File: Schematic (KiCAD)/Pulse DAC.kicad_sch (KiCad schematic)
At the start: 72 parts

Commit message: - Pulse DAC logic is now complete.  - The 4-bit adders are verified correct using Excel.    - This revealed 1 tracing error and also 3 XNOR gates that are actually XOR in this case.  - Now including a PDF version of the schematic.
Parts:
- removed B72, B80: XNOR_2, symbol MMC5:XNOR_2
- added B46, B63, B66, B67, B71, B79, B87, B88, B89, B94, C13, F29, G17: INVERT, symbol MMC5:INVERT
- added B62: NOR_4, symbol MMC5:NOR_4
- added B64, B70, B74, B76, B77, B78, B83, B86, G27, G88: NAND_2, symbol MMC5:NAND_2
- added B65, B68: NAND_3, symbol MMC5:NAND_3
- added B72, B80: XOR_2, symbol MMC5:XOR_2
- added B75: NOR_3, symbol MMC5:NOR_3
- added B81, B82: NOR_2, symbol MMC5:NOR_2
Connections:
- net Pulse_1_With_Duty{F32}: now also G88. (X)
- net Pulse_2_With_Duty{G20}: now also G27. (X)
- net Pulse_DAC_Bit_4: now also B80. (X); no longer B61. (X)
- net Pulse_DAC_Bit_5: now also B72. (X)
- net Pulse_DAC_Bit_7: now also B61. (X)
- net Pulse_1_DAC.2{F30}: now reaches F30. (X)
- net Pulse_1_DAC.2{F30}: now also B73. (X), B74. (X); no longer G89. (X)
- net at H45. (X): now also H66. (X); no longer H44. (X)
- net at H66. (X): now also H63. (X); no longer H45. (X)
- net Pulse_DACs_Nor.0{B84}: now reaches B54. (X)
- net Pulse_DACs_Nor.0{B84}: now also B50. (X), B84. (X), B65. (X), B76. (X), B81. (X)
- net at B59. (X): now also B61. (X); no longer B54. (X)
- net at H71. (X): now also H74. (X); no longer H70. (X)
- net at H74. (X): now also H75. (X); no longer H71. (X)
- net at H73. (X): now also H72. (X); no longer H74. (X)
- net at H47. (X): now also H46. (X); no longer H74. (X)
- net at H75. (X): now also H80. (/Q3); no longer H74. (X)
- net at H58. (X): now also H80. (/Q3); no longer H57. (X)
- net Pulse_DACs_Nor.3{B53}: now reaches B61. (X)
- net Pulse_DACs_Nor.3{B53}: now also B53. (X), C13. (X); no longer B59. (X)
- net at B57. (X): now also B61. (X); no longer B56. (X)
- net at H43. (X): now also H42. (X); no longer H57. (X)
- net Pulse_2_DAC.2{G18}: now reaches B73. (X), G18. (X)
- net Pulse_2_DAC.2{G18}: now also B74. (X)
- net Pulse_DACs_Nor.2{B73}: now reaches B73. (X)
- net Pulse_DACs_Nor.2{B73}: now also B56. (X), B62. (X), B87. (X); no longer F30. (X)
- net at H49. (X): now also H50. (X); no longer H48. (X)
- net at H50. (X): now also H51. (X); no longer H41. (X)
- net at H51. (X): now also H80. (/Q3); no longer H50. (X)
- net at H57. (X): now also H56. (X); no longer H54. (X)
- net at H56. (X): now also H55. (X); no longer H57. (X)
- net Pulse_2_DAC.3{G19}: now reaches G19. (X)
- net Pulse_2_DAC.3{G19}: now also B45. (X), B53. (X); no longer G25. (X)
- net Pulse_2_DAC.0{G24}: now reaches G24. (X)
- net Pulse_2_DAC.0{G24}: now also B84. (X), B85. (X); no longer G28. (X)
- net Pulse_DACs_Nand.3{B45}: now reaches B45. (X), B56. (X)
- net Pulse_DACs_Nand.3{B45}: now also B52. (X), B54. (X), B55. (X), B86. (X)
- net Pulse_1_DAC.3{F31}: now reaches B45. (X), F31. (X)
- net Pulse_1_DAC.3{F31}: now also B53. (X)
- net at H67. (X): now also H66. (X); no longer H80. (/Q3)
- net Pulse_DACs_Nor.1{B82}: now reaches B55. (X)
- net Pulse_DACs_Nor.1{B82}: now also B64. (X), B75. (X), B82. (X), B88. (X)
- net at B58. (X): now also B61. (X); no longer B55. (X)
- net Pulse_DACs_Nand.0{B85}: now reaches B49. (X), B85. (X)
- net Pulse_DACs_Nand.0{B85}: now also B52. (X), B68. (X), B77. (X), B81. (X)
- net Pulse_1_DAC.0{F28}: now reaches F28. (X)
- net Pulse_1_DAC.0{F28}: now also B84. (X), B85. (X); no longer G87. (X)
- net at H65. (X): now also H64. (X); no longer H66. (X)
- net at B60. (X): now also B61. (X); no longer B52. (X)
- new net: F30. (X), G89. (X)
- new net: H44. (X), H45. (X)
- new net: B54. (X), B59. (X)
- new net: B72. (X), B75. (X)
- new net: B75. (X), B94. (X)
- new net: B75. (X), B89. (X)
- new net: H38. (X), H48. (X), H53. (X), H55. (X), H61. (X), H62. (X), H64. (X), H69. (X), H70. (X), H72. (X)
- new net: H70. (X), H71. (X)
- new net: H69. (X), H70. (X)
- new net: H38. (X), H39. (X), H40. (X), H42. (X), H44. (X), H46. (X)
- new net: B86. (X), C13. (X)
- new net: H73. (X), H74. (X)
- new net: H47. (X), H74. (X)
- new net: H57. (X), H58. (X)
- new net: B56. (X), B57. (X)
- new net: H43. (X), H57. (X)
- new net: B76. (X), B94. (X)
- new net: B78. (X), B88. (X)
- new net: B47. (X), B62. (X)
- new net: B46. (X), B47. (X)
- new net: B71. (X), B72. (X)
- new net: B70. (X), B71. (X)
- new net: H61. (X), H62. (X)
- new net: H62. (X), H63. (X)
- new net: H48. (X), H49. (X)
- new net: H41. (X), H50. (X)
- new net: H54. (X), H57. (X)
- new net: G18. (X), G26. (X)
- new net: G19. (X), G25. (X)
- new net: F29. (X), G88. (X)
- new net: G24. (X), G28. (X)
- new net: B63. (X), B64. (X)
- new net: B62. (X), B63. (X)
- new net: B70. (X), B87. (X)
- new net: B80. (X), B81. (X)
- new net: B67. (X), B68. (X)
- new net: B62. (X), B67. (X)
- new net: H67. (X), H80. (/Q3)
- new net: B46. (X), B86. (X)
- new net: B55. (X), B58. (X)
- new net: B77. (X), B89. (X)
- new net: B65. (X), B66. (X)
- new net: B62. (X), B66. (X)
- new net: F28. (X), G87. (X)
- new net: B79. (X), B80. (X)
- new net: G17. (X), G27. (X)
- new net: H65. (X), H66. (X)
- new net: B52. (X), B60. (X)
- new net: F31. (X), G90. (X)
- new net: B49. (X), B51. (X)
- new net: B49. (X), B50. (X)
- new net: B78. (X), B79. (X)
- new net Pulse_1_DAC.1{F29}: B82. (X), B83. (X), F29. (X)
- new net Pulse_1_Vol/Env.1{H102}: G88. (X)
- new net Pulse_2_DAC.1{G17}: B82. (X), B83. (X), G17. (X)
- new net Pulse_2_Vol/Env.1{F23}: G27. (X)
- new net Pulse_DACs_Nand.1{B83}: B52. (X), B54. (X), B65. (X), B68. (X), B76. (X), B77. (X), B78. (X), B83. (X)
- new net Pulse_DACs_Nand.2{B74}: B52. (X), B54. (X), B55. (X), B64. (X), B65. (X), B68. (X), B70. (X), B74. (X)
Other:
- note added: "$5015 Write Register Pulse 1&2 Status"
- note added: "4-bit Adder Adding Pulse 1&2 DACs"
- note added: "B80,B72,B47: Though they look like XNOR gates from elsewhere, logically these must be XOR."
- note added: "Components for 4-bit Adder"
- note added: "Don't know what this is yet But it is important."
- note added: "Note: The adder's logic is verified correct in Pulse DAC Adder Logic.xlsx"
- note added: "Pulse 1&2 Individual 4-bit DAC Outputs"
- note added: "This logic amounts to XOR"
- note removed: "$5015 Register Pulse 1&2 Status"
- moved on the sheet: B45, B47, B49, B50, B51, B52, B53, B54, B55, B56, B57, B58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

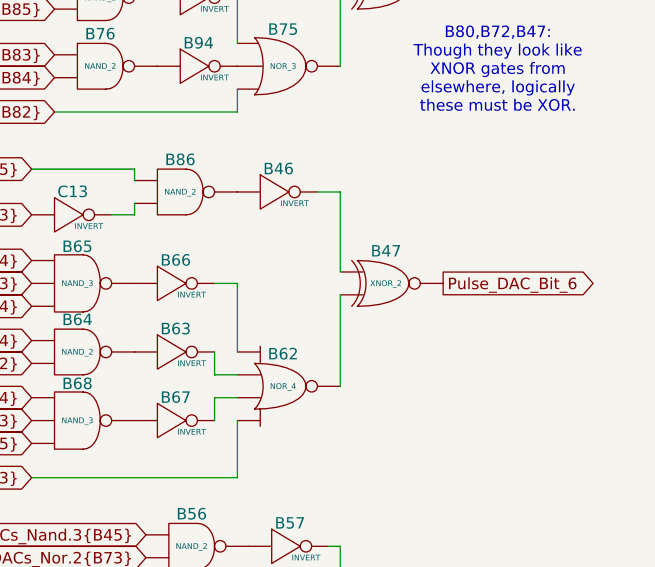
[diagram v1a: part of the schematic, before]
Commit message: Schematic Updates:  - Added all 10-bit CHR banking registers $5120 - $512B, including where all 10 bits come from when written.  - Added 8-bit CHR bank register $5202, which is the bank used when rendering the V-Split region.    + V-Split seems to always be 8-bit, 8kB bank regardless of CHR mode.  The wiki doesn't say that and I don't know for sure.  - Added decoding logic that activates the correct CHR bank for CHR A10, A11, A12 (corresponding to columns AV, AW, AX).  - Noted, AX15 activates $5202 CHR Bank for V-Split region.  AX16 activates CHR Bank from data stored in ExRAM for extended attributes.  Therefore, AX15 driven by AT1 High means we specifically are in v-split region, and not extended attribute mode.  With this knowledge, backtracking up the chain from AT1 to N14 sheds very useful insight what the 3-bit shift register at N11/N12/N13 is doing.  We now know that N14 goes low specifically for pattern table fetches when rendering the V-split region, and does not appear dual-purposed for extended attribute fetch sequencing.  This may seem rather subtle or unimportant, but it is a good advancement for higher level understanding what that mysterious shift register might be doing.
SVG Trace Updates:
 - Registers $5120, 5121, 5122, 5123 (first 4 CHR bank register), the outputs were labeled in reverse order.
 - Register $5130 (highest CHR bank bits), the outputs were labeled with backwards polarity.  The error was not having taken into account that the CPU data bus input to the latches came already inverted to begin with.
 - Still wrong: Cell AV7, 2-input NAND gate.  One of the inputs is missing and it logically should be driven by AS19 like the 4 cells to its direct right.  I can't quite make out how it makes that connection.
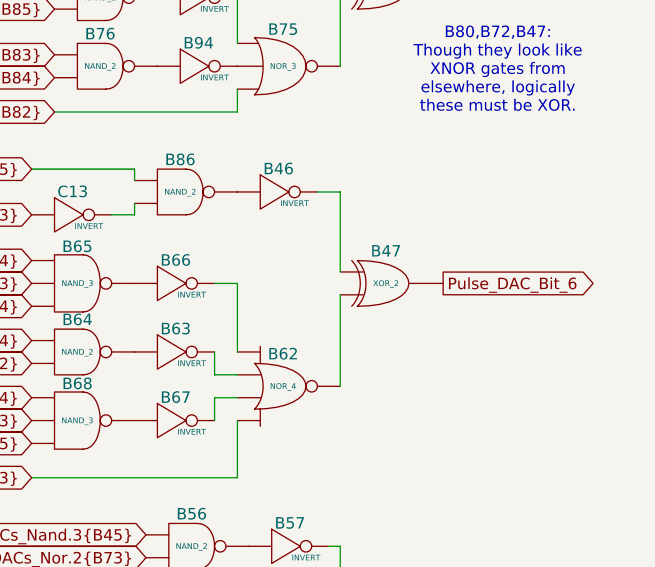
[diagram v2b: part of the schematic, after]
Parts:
- removed B47: XNOR_2, symbol MMC5:XNOR_2
- added B47: XOR_2, symbol MMC5:XOR_2
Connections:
- net Pulse_DAC_Bit_6: now also B47. (X)
- net at H45. (X): now also H66. (X); no longer H44. (X)
- net at H66. (X): now also H63. (X); no longer H45. (X)
- net at B59. (X): now also B61. (X); no longer B54. (X)
- net at B94. (X): now also B76. (X); no longer B75. (X)
- net at B89. (X): now also B77. (X); no longer B75. (X)
- net at H71. (X): now also H74. (X); no longer H70. (X)
- net at H74. (X): now also H75. (X); no longer H71. (X)
- net at H73. (X): now also H72. (X); no longer H74. (X)
- net at H47. (X): now also H46. (X); no longer H74. (X)
- net at H75. (X): now also H80. (/Q3); no longer H74. (X)
- net at H58. (X): now also H80. (/Q3); no longer H57. (X)
- net at B57. (X): now also B61. (X); no longer B56. (X)
- net at H43. (X): now also H42. (X); no longer H57. (X)
- net at B46. (X): now also B86. (X)
- net at B71. (X): now also B70. (X); no longer B72. (X)
- net at H49. (X): now also H50. (X); no longer H48. (X)
- net at H50. (X): now also H51. (X); no longer H41. (X)
- net at H51. (X): now also H80. (/Q3); no longer H50. (X)
- net at H57. (X): now also H56. (X); no longer H54. (X)
- net at H56. (X): now also H55. (X); no longer H57. (X)
- net at B63. (X): now also B62. (X); no longer B64. (X)
- net at B67. (X): now also B62. (X); no longer B68. (X)
- net at H67. (X): now also H66. (X); no longer H80. (/Q3)
- net at B58. (X): now also B61. (X); no longer B55. (X)
- net at B66. (X): now also B62. (X); no longer B65. (X)
- net at B79. (X): now also B78. (X); no longer B80. (X)
- net at H65. (X): now also H64. (X); no longer H66. (X)
- net at B60. (X): now also B61. (X); no longer B52. (X)
- new net: F30. (X), G89. (X)
- new net: H44. (X), H45. (X)
- new net: B54. (X), B59. (X)
- new net: B72. (X), B75. (X)
- new net: B75. (X), B94. (X)
- new net: B75. (X), B89. (X)
- new net: H38. (X), H48. (X), H53. (X), H55. (X), H61. (X), H62. (X), H64. (X), H69. (X), H70. (X), H72. (X)
- new net: H70. (X), H71. (X)
- new net: H69. (X), H70. (X)
- new net: H38. (X), H39. (X), H40. (X), H42. (X), H44. (X), H46. (X)
- new net: B86. (X), C13. (X)
- new net: H73. (X), H74. (X)
- new net: H47. (X), H74. (X)
- new net: H57. (X), H58. (X)
- new net: B56. (X), B57. (X)
- new net: H43. (X), H57. (X)
- new net: B78. (X), B88. (X)
- new net: B71. (X), B72. (X)
- new net: H61. (X), H62. (X)
- new net: H62. (X), H63. (X)
- new net: H48. (X), H49. (X)
- new net: H41. (X), H50. (X)
- new net: H54. (X), H57. (X)
- new net: G18. (X), G26. (X)
- new net: B47. (X), B62. (X)
- new net: B46. (X), B47. (X)
- new net: G19. (X), G25. (X)
- new net: F29. (X), G88. (X)
- new net: G24. (X), G28. (X)
- new net: B63. (X), B64. (X)
- new net: B70. (X), B87. (X)
- new net: B80. (X), B81. (X)
- new net: B67. (X), B68. (X)
- new net: H67. (X), H80. (/Q3)
- new net: B55. (X), B58. (X)
- new net: B65. (X), B66. (X)
- new net: F28. (X), G87. (X)
- new net: B79. (X), B80. (X)
- new net: G17. (X), G27. (X)
- new net: H65. (X), H66. (X)
- new net: B52. (X), B60. (X)
- new net: F31. (X), G90. (X)
- new net: B49. (X), B51. (X)
- new net: B49. (X), B50. (X)

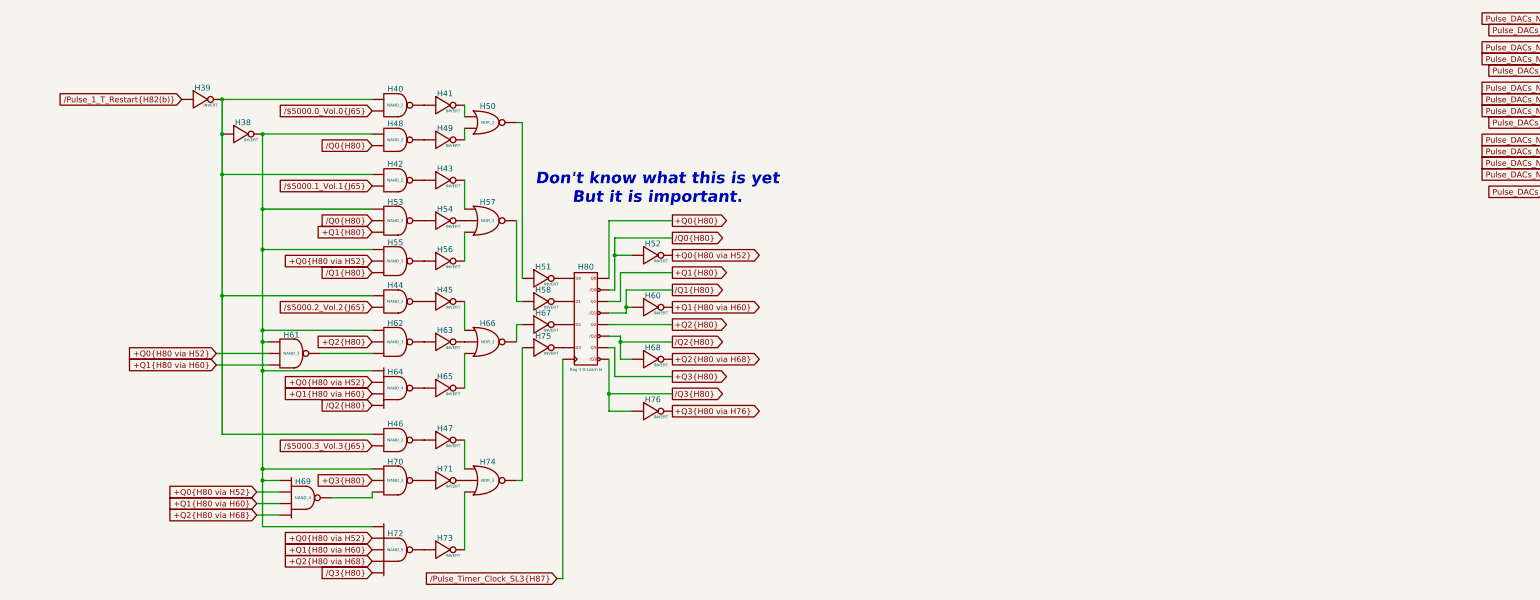
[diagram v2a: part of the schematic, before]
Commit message: - All cells in the left and center areas have now been added into the schematics.  - Changed naming of the PDF files; I was accidentally writing over furrtek's original with my new PDF.
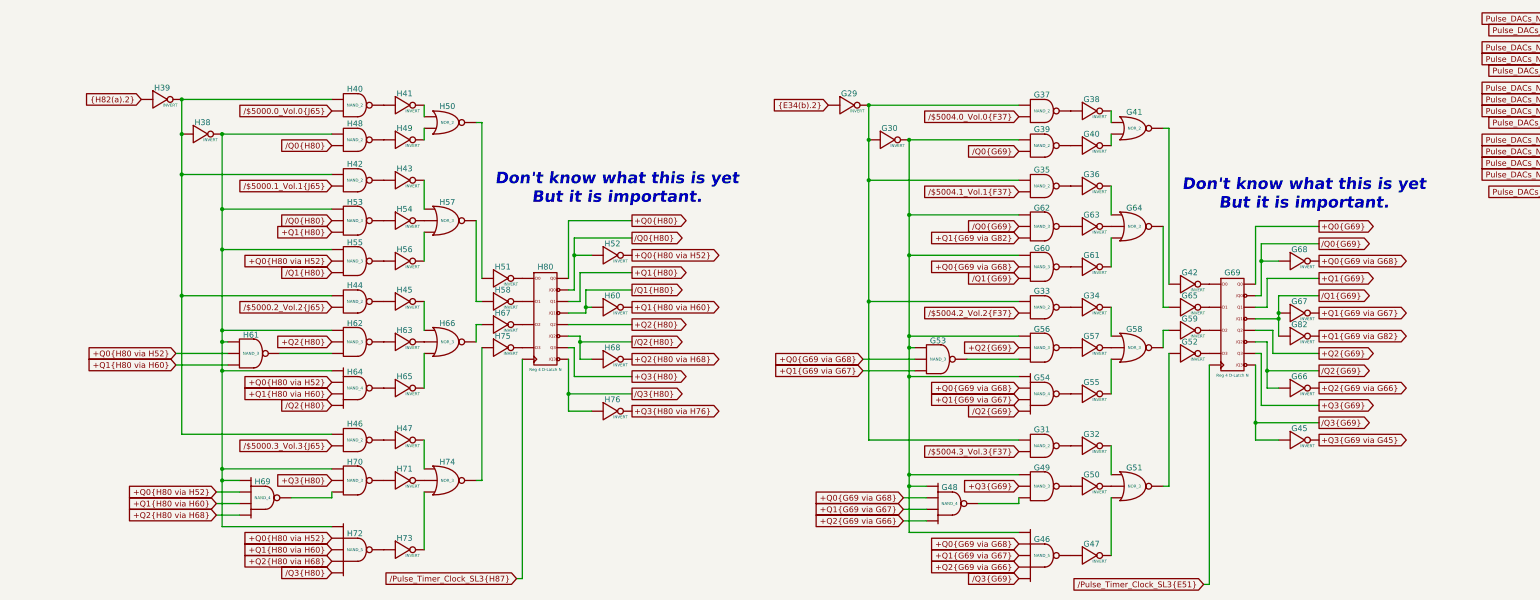
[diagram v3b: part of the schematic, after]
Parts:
- added G29, G30, G32, G34, G36, G38, G40, G42, G45, G47, G50, G52, G55, G57, G59, G61, G63, G65, G66, G67, G68, G82: INVERT, symbol MMC5:INVERT
- added G31, G33, G35, G37, G39: NAND_2, symbol MMC5:NAND_2
- added G41: NOR_2, symbol MMC5:NOR_2
- added G46: NAND_5, symbol MMC5:NAND_5
- added G48, G54: NAND_4, symbol MMC5:NAND_4
- added G49, G53, G56, G60, G62: NAND_3, symbol MMC5:NAND_3
- added G51, G58, G64: NOR_3, symbol MMC5:NOR_3
- added G69: Reg 4 D-Latch N, symbol MMC5:Reg_4_D-Latch_N
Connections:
- net at H45. (X): now also H66. (X); no longer H44. (X)
- net at H66. (X): now also H63. (X); no longer H45. (X)
- net at B59. (X): now also B61. (X); no longer B54. (X)
- net at B94. (X): now also B76. (X); no longer B75. (X)
- net at B89. (X): now also B77. (X); no longer B75. (X)
- net at H71. (X): now also H74. (X); no longer H70. (X)
- net at H74. (X): now also H75. (X); no longer H71. (X)
- net at H73. (X): now also H72. (X); no longer H74. (X)
- net at H47. (X): now also H46. (X); no longer H74. (X)
- net at H75. (X): now also H80. (/Q3); no longer H74. (X)
- net at H58. (X): now also H80. (/Q3); no longer H57. (X)
- net at B57. (X): now also B61. (X); no longer B56. (X)
- net at H43. (X): now also H42. (X); no longer H57. (X)
- net at B71. (X): now also B70. (X); no longer B72. (X)
- net at H49. (X): now also H50. (X); no longer H48. (X)
- net at H50. (X): now also H51. (X); no longer H41. (X)
- net at H51. (X): now also H80. (/Q3); no longer H50. (X)
- net at H57. (X): now also H56. (X); no longer H54. (X)
- net at H56. (X): now also H55. (X); no longer H57. (X)
- net at B46. (X): now also B86. (X); no longer B47. (X)
- net at B63. (X): now also B62. (X); no longer B64. (X)
- net at B67. (X): now also B62. (X); no longer B68. (X)
- net at H67. (X): now also H66. (X); no longer H80. (/Q3)
- net at B58. (X): now also B61. (X); no longer B55. (X)
- net at B66. (X): now also B62. (X); no longer B65. (X)
- net at B79. (X): now also B78. (X); no longer B80. (X)
- net at H65. (X): now also H64. (X); no longer H66. (X)
- net at B60. (X): now also B61. (X); no longer B52. (X)
- net /Pulse_1_T_Restart{H82(b)} renamed {H82(a).2}
- new net: F30. (X), G89. (X)
- new net: H44. (X), H45. (X)
- new net: B54. (X), B59. (X)
- new net: B72. (X), B75. (X)
- new net: B75. (X), B94. (X)
- new net: B75. (X), B89. (X)
- new net: G47. (X), G51. (X)
- new net: G46. (X), G47. (X)
- new net: H38. (X), H48. (X), H53. (X), H55. (X), H61. (X), H62. (X), H64. (X), H69. (X), H70. (X), H72. (X)
- new net: H70. (X), H71. (X)
- new net: H69. (X), H70. (X)
- new net: H38. (X), H39. (X), H40. (X), H42. (X), H44. (X), H46. (X)
- new net: B86. (X), C13. (X)
- new net: G62. (X), G63. (X)
- new net: G63. (X), G64. (X)
- new net: H73. (X), H74. (X)
- new net: H47. (X), H74. (X)
- new net: G34. (X), G58. (X)
- new net: G58. (X), G59. (X)
- new net: G55. (X), G58. (X)
- new net: G57. (X), G58. (X)
- new net: H57. (X), H58. (X)
- new net: B56. (X), B57. (X)
- new net: H43. (X), H57. (X)
- new net: G33. (X), G34. (X)
- new net: G30. (X), G39. (X), G46. (X), G48. (X), G49. (X), G53. (X), G54. (X), G56. (X), G60. (X), G62. (X)
- new net: G39. (X), G40. (X)
- new net: B78. (X), B88. (X)
- new net: B71. (X), B72. (X)
- new net: H61. (X), H62. (X)
- new net: H62. (X), H63. (X)
- new net: H48. (X), H49. (X)
- new net: H41. (X), H50. (X)
- new net: G37. (X), G38. (X)
- new net: G38. (X), G41. (X)
- new net: G49. (X), G50. (X)
- new net: G48. (X), G49. (X)
- new net: G50. (X), G51. (X)
- new net: G51. (X), G52. (X)
- new net: G32. (X), G51. (X)
- new net: G53. (X), G56. (X)
- new net: H54. (X), H57. (X)
- new net: G18. (X), G26. (X)
- new net: G29. (X), G30. (X), G31. (X), G33. (X), G35. (X), G37. (X)
- new net: B47. (X), B62. (X)
- new net: B46. (X), B47. (X)
- new net: G19. (X), G25. (X)
- new net: G35. (X), G36. (X)
- new net: G36. (X), G64. (X)
- new net: F29. (X), G88. (X)
- new net: G24. (X), G28. (X)
- new net: B63. (X), B64. (X)
- new net: B70. (X), B87. (X)
- new net: B80. (X), B81. (X)
- new net: B67. (X), B68. (X)
- new net: H67. (X), H80. (/Q3)
- new net: B55. (X), B58. (X)
- new net: G60. (X), G61. (X)
- new net: B65. (X), B66. (X)
- new net: F28. (X), G87. (X)
- new net: B79. (X), B80. (X)
- new net: G17. (X), G27. (X)
- new net: G56. (X), G57. (X)
- new net: G61. (X), G64. (X)
- new net: G64. (X), G65. (X)
- new net: G31. (X), G32. (X)
- new net: G52. (X), G69. (/Q3)
- new net: H65. (X), H66. (X)
- new net: G59. (X), G69. (/Q3)
- new net: G42. (X), G69. (/Q3)
- new net: G65. (X), G69. (/Q3)
- new net: B52. (X), B60. (X)
- new net: F31. (X), G90. (X)
- new net: B49. (X), B51. (X)
- new net: B49. (X), B50. (X)
- new net: G54. (X), G55. (X)
- new net: G41. (X), G42. (X)
- new net: G40. (X), G41. (X)
- new net +Q0{G69 via G68}: G46. (X), G48. (X), G53. (X), G54. (X), G60. (X), G68. (X)
- new net +Q0{G69}: G69. (/Q3)
- new net +Q1{G69 via G67}: G46. (X), G48. (X), G53. (X), G54. (X), G67. (X)
- new net +Q1{G69 via G82}: G62. (X), G82. (X)
- new net +Q1{G69}: G69. (/Q3)
- new net +Q2{G69 via G66}: G46. (X), G48. (X), G66. (X)
- new net +Q2{G69}: G56. (X), G69. (/Q3)
- new net +Q3{G69 via G45}: G45. (X)
- new net +Q3{G69}: G49. (X), G69. (/Q3)
- new net {E34(b).2}: G29. (X)
- new net /$5004.0_Vol.0{F37}: G37. (X)
- new net /$5004.1_Vol.1{F37}: G35. (X)
- new net /$5004.2_Vol.2{F37}: G33. (X)
- new net /$5004.3_Vol.3{F37}: G31. (X)
- new net /Pulse_Timer_Clock_SL3{E51}: G69. (/Q3)
- new net /Q0{G69}: G39. (X), G62. (X), G68. (X), G69. (/Q3)
- new net /Q1{G69}: G60. (X), G67. (X), G69. (/Q3), G82. (X)
- new net /Q2{G69}: G54. (X), G66. (X), G69. (/Q3)
- new net /Q3{G69}: G45. (X), G46. (X), G69. (/Q3)
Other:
- moved on the sheet: H38, H39, H40, H41, H42, H43, H44, H45, H46, H47, H48, H49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
